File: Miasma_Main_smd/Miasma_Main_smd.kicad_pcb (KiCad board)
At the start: 2 copper layers, 99.1 x 99.1 mm, 168 parts, among them P1 CONN_01X12, P2 CONN_01X10, P3 CONN_01X12, P4 CONN_01X10, P5 CONN_02X05, P6 CONN_01X01, P7 SUM_or_4QX, Q1 MMBT3904, Q2 MMBT3904, Q3 MMBT3904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

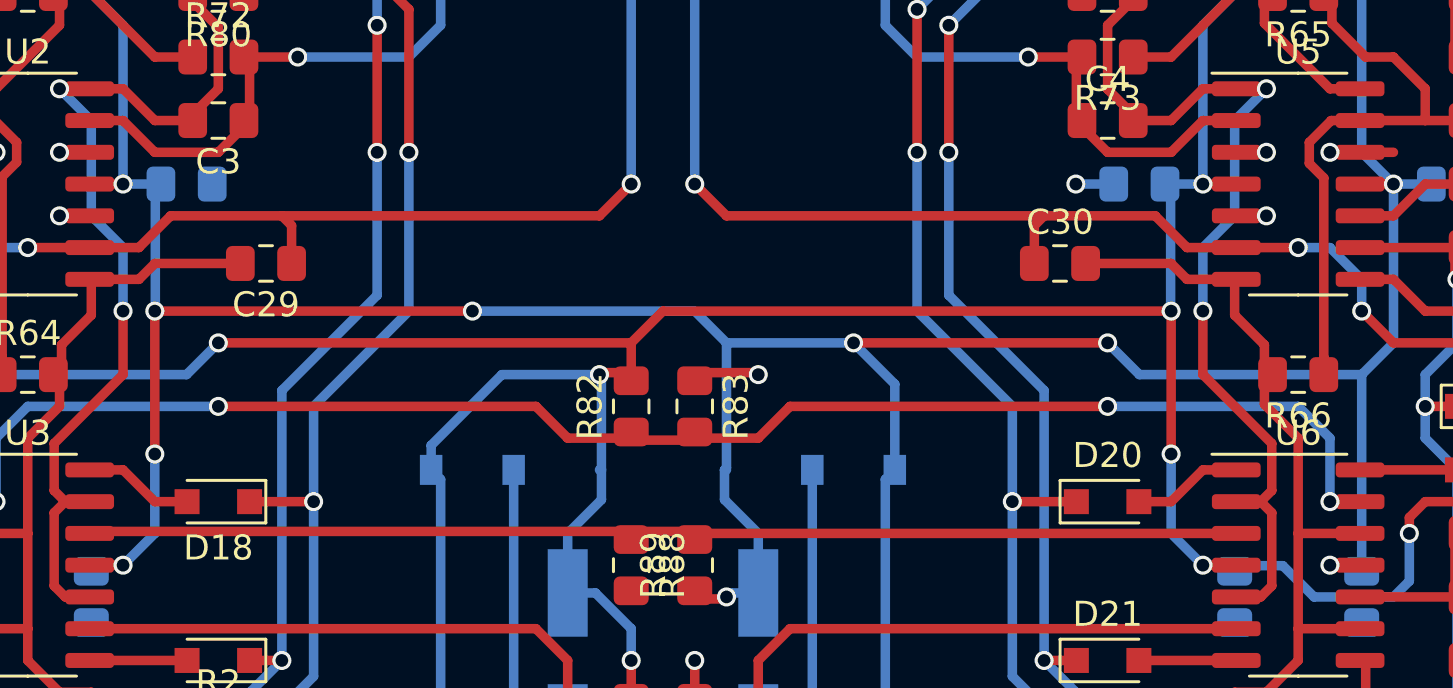
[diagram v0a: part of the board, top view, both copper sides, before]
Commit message: Added through-hole footprints for C7/C8 (polypropylene timing caps)
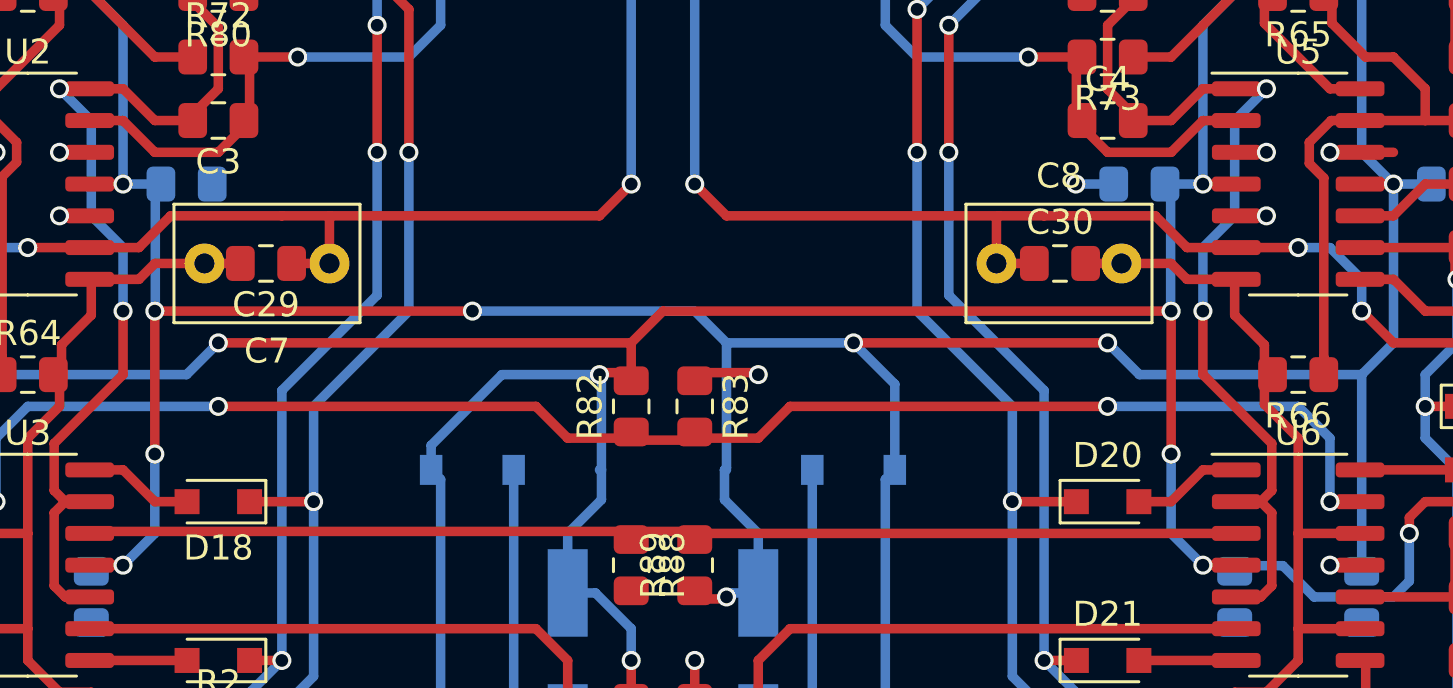
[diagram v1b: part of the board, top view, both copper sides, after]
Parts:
- added C7: 2n2 (PP), Capacitor_THT:C_Rect_L7.2mm_W4.5mm_P5.00mm_FKS2_FKP2_MKS2_MKP2, F.Cu at (131.4, 78.1)
- added C8: 2n2 (PP), Capacitor_THT:C_Rect_L7.2mm_W4.5mm_P5.00mm_FKS2_FKP2_MKS2_MKP2, F.Cu at (158.1, 78.1)
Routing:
- net RngCap2: track 99.2 -> 100.6 mm
- net RngCap1: track 92.6 -> 93.9 mm
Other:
- board text added: "SUM"
